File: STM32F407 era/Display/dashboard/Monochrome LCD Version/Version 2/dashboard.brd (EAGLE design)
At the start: 200 x 75.1 mm, 89 parts, among them IC2 74HC14D, IC3 74HC14D, U1 CAT4238TD-GT3

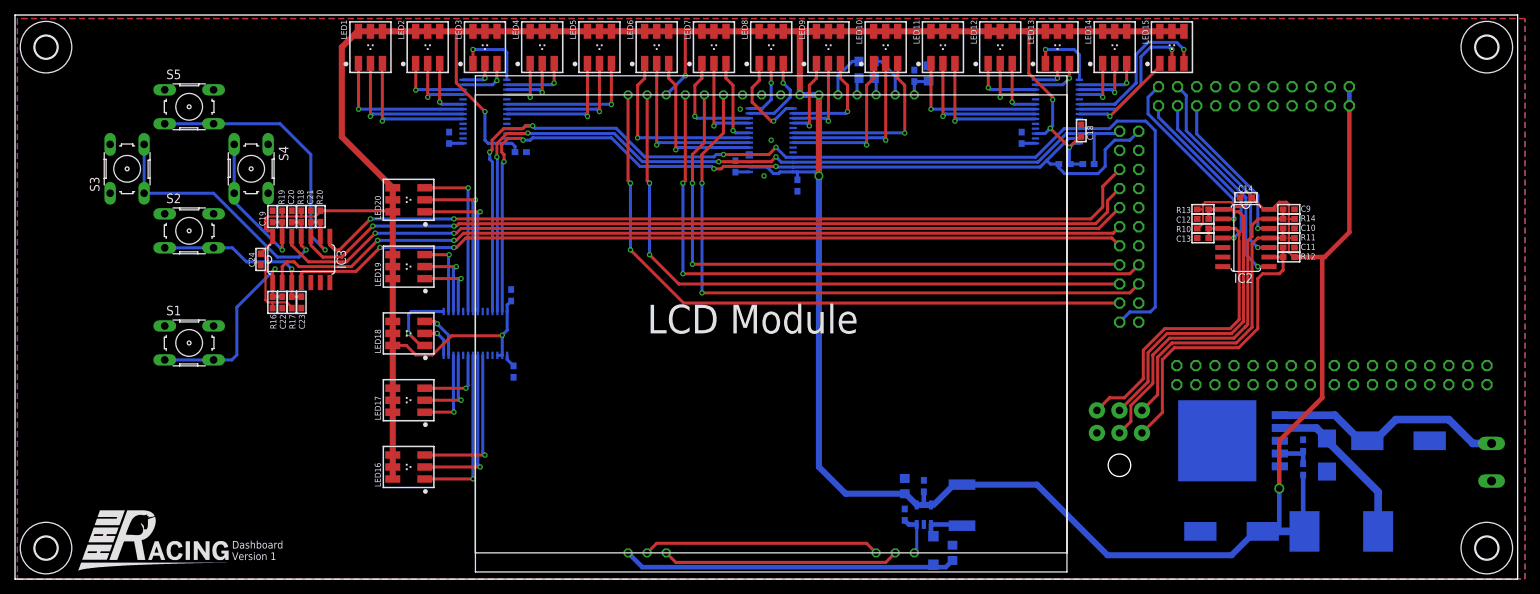
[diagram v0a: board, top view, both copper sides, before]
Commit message: fixed silkscreen and added extra button for interface
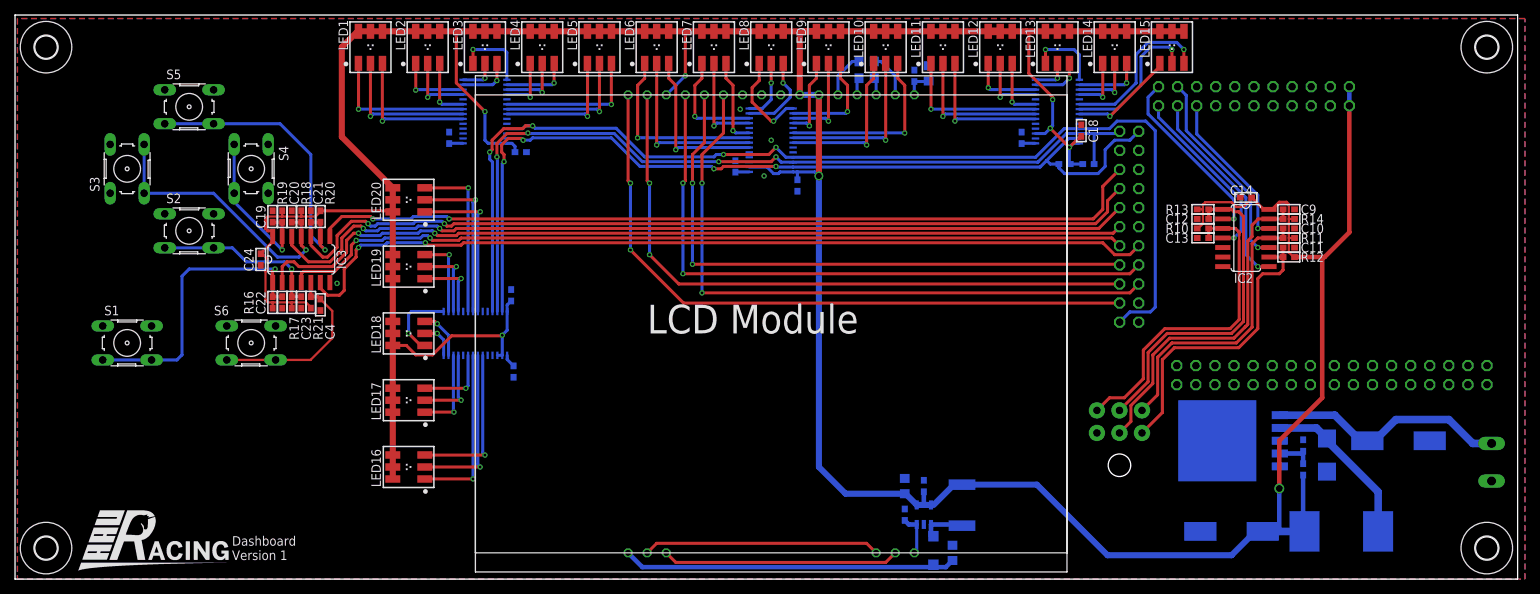
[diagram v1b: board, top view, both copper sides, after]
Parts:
- added C4: 100n, microbuilder:_0603
- added R21: 500, microbuilder:_0603
- added S6: (no value), switch-omron:B3F-10XX
- moved S1 8.26 mm to (58.1, 47.9)
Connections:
- new net SW6: C4.2, IC3.5, R21.1, S6.3, S6.4
- new net SW6S: IC3.6, U$1.P$10
- net 3.3V: now also R21.2
- net GND: now also C4.1, S6.1, S6.2; no longer IC3.5
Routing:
- net SW6S: track 0.00 -> 116.6 mm, vias 0 -> 2
- net SW6: track 0.00 -> 24.4 mm
- net SW1: track 28.5 -> 39.2 mm
- net 3.3V: track 543.4 -> 546.7 mm
- net SW3S: track 114.1 -> 116.1 mm
- net SW4S: track 115.3 -> 117.3 mm
- net SW1S: track 116.3 -> 118.0 mm
- net SW2S: track 112.5 -> 113.8 mm
- net SW5S: track 112.6 -> 111.7 mm

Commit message: started work on V2
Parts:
- moved U$42 5.46 mm to (193.4, 33.0), turned to 90 degrees
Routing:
- net BTN5: track 40.7 -> 53.8 mm
- net BTN3: track 39.0 -> 49.5 mm
- net BTN4: track 45.7 -> 54.4 mm
- net BTN1: track 47.3 -> 53.4 mm
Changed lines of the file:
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@@
 <attribute name="VALUE" x="166.4335" y="85.4074" size="0.4064" layer="28" ratio="10" rot="MR270"/>
 </element>
-<element name="U$42" library="unicorn" package="MICROFIT6SOCK" value="MICROFIT6" x="190.1825" y="37.465" rot="MR0"/>
+<element name="U$42" library="unicorn" package="MICROFIT6SOCK" value="MICROFIT6" x="193.3575" y="33.02" rot="MR90"/>
 <element name="R10" library="microbuilder" package="_0603" value="500" x="201.295" y="63.1825" smashed="yes" rot="R180">
 <attribute name="NAME" x="199.39" y="63.8175" size="1.27" layer="25" ratio="18" rot="R180"/>
@@
 <wire x1="205.74" y1="47.9425" x2="197.1675" y2="47.9425" width="0.4064" layer="1"/>
 <wire x1="197.1675" y1="47.9425" x2="195.2625" y2="46.0375" width="0.4064" layer="1"/>
-<wire x1="195.2625" y1="46.0375" x2="195.2625" y2="41.045" width="0.4064" layer="1"/>
-<wire x1="195.2625" y1="41.045" x2="193.1825" y2="38.965" width="0.4064" layer="1"/>
+<wire x1="195.2625" y1="46.0375" x2="195.2625" y2="39.6875" width="0.4064" layer="1"/>
 <wire x1="207.8355" y1="50.038" x2="205.74" y2="47.9425" width="0.4064" layer="1"/>
 <wire x1="210.0834" y1="61.9125" x2="208.5975" y2="61.9125" width="0.4064" layer="1"/>
 <wire x1="208.5975" y1="61.9125" x2="207.8355" y2="61.1505" width="0.4064" layer="1"/>
 <wire x1="207.8355" y1="61.1505" x2="207.8355" y2="50.038" width="0.4064" layer="1"/>
+<wire x1="195.2625" y1="39.6875" x2="197.8025" y2="37.1475" width="0.4064" layer="1"/>
+<wire x1="197.8025" y1="37.1475" x2="197.8025" y2="32.7025" width="0.4064" layer="1"/>
+<wire x1="197.8025" y1="32.7025" x2="195.58" y2="30.48" width="0.4064" layer="1"/>
+<wire x1="195.58" y1="30.48" x2="195.3175" y2="30.48" width="0.4064" layer="1"/>
+<wire x1="195.3175" y1="30.48" x2="194.8575" y2="30.02" width="0.4064" layer="1"/>
 </signal>
 <signal name="BTN2">
@@
 <wire x1="203.9366" y1="63.1825" x2="202.057" y2="63.1825" width="0.3048" layer="1"/>
 <wire x1="202.057" y1="63.1825" x2="202.057" y2="61.9125" width="0.4064" layer="1"/>
-<wire x1="187.1825" y1="38.965" x2="188.8575" y2="40.64" width="0.4064" layer="1"/>
-<wire x1="188.8575" y1="40.64" x2="190.8175" y2="40.64" width="0.4064" layer="1"/>
-<wire x1="190.8175" y1="40.64" x2="193.3575" y2="43.18" width="0.4064" layer="1"/>
-<wire x1="193.3575" y1="43.18" x2="193.3575" y2="46.99" width="0.4064" layer="1"/>
 <wire x1="193.3575" y1="46.99" x2="196.215" y2="49.8475" width="0.4064" layer="1"/>
 <wire x1="196.215" y1="49.8475" x2="204.9145" y2="49.8475" width="0.4064" layer="1"/>
@@
 <wire x1="206.121" y1="62.2935" x2="206.121" y2="61.5315" width="0.3048" layer="1"/>
 <wire x1="206.121" y1="61.5315" x2="206.121" y2="51.054" width="0.4064" layer="1"/>
+<wire x1="193.3575" y1="46.99" x2="193.3575" y2="37.52" width="0.4064" layer="1"/>
+<wire x1="193.3575" y1="37.52" x2="194.8575" y2="36.02" width="0.4064" layer="1"/>
 </signal>
 <signal name="BTN1">
@@
 <wire x1="205.105" y1="49.2125" x2="196.5325" y2="49.2125" width="0.4064" layer="1"/>
 <wire x1="196.5325" y1="49.2125" x2="193.9925" y2="46.6725" width="0.4064" layer="1"/>
-<wire x1="193.9925" y1="46.6725" x2="193.9925" y2="42.775" width="0.4064" layer="1"/>
-<wire x1="193.9925" y1="42.775" x2="190.1825" y2="38.965" width="0.4064" layer="1"/>
+<wire x1="193.9925" y1="46.6725" x2="193.9925" y2="39.0525" width="0.4064" layer="1"/>
 <wire x1="206.6925" y1="50.8" x2="205.105" y2="49.2125" width="0.4064" layer="1"/>
 <wire x1="206.6925" y1="50.8" x2="206.6925" y2="64.77" width="0.4064" layer="1"/>
 <wire x1="206.6925" y1="64.77" x2="206.0575" y2="65.405" width="0.4064" layer="1"/>
+<wire x1="193.9925" y1="39.0525" x2="196.5325" y2="36.5125" width="0.4064" layer="1"/>
+<wire x1="196.5325" y1="36.5125" x2="196.5325" y2="34.695" width="0.4064" layer="1"/>
+<wire x1="196.5325" y1="34.695" x2="194.8575" y2="33.02" width="0.4064" layer="1"/>
 </signal>
 <signal name="BTN4">
@@
 <wire x1="205.4225" y1="48.5775" x2="196.85" y2="48.5775" width="0.4064" layer="1"/>
 <wire x1="196.85" y1="48.5775" x2="194.6275" y2="46.355" width="0.4064" layer="1"/>
-<wire x1="194.6275" y1="46.355" x2="194.6275" y2="42.545" width="0.4064" layer="1"/>
-<wire x1="194.6275" y1="42.545" x2="191.7065" y2="39.624" width="0.4064" layer="1"/>
-<wire x1="191.7065" y1="39.624" x2="191.7065" y2="37.489" width="0.4064" layer="1"/>
-<wire x1="191.7065" y1="37.489" x2="190.1825" y2="35.965" width="0.4064" layer="1"/>
-<wire x1="207.01" y1="50.165" x2="206.91475" y2="50.06975" width="0.4064" layer="1"/>
-<wire x1="206.91475" y1="50.06975" x2="205.4225" y2="48.5775" width="0.4064" layer="1"/>
+<wire x1="194.6275" y1="46.355" x2="194.6275" y2="39.37" width="0.4064" layer="1"/>
+<wire x1="207.264" y1="50.419" x2="205.4225" y2="48.5775" width="0.4064" layer="1"/>
 <wire x1="210.0834" y1="64.4525" x2="208.661" y2="64.4525" width="0.4064" layer="1"/>
 <wire x1="208.661" y1="64.4525" x2="207.8355" y2="63.627" width="0.4064" layer="1"/>
@@
 <wire x1="207.8355" y1="62.103" x2="207.264" y2="61.5315" width="0.4064" layer="1"/>
 <wire x1="207.264" y1="61.5315" x2="207.264" y2="50.419" width="0.4064" layer="1"/>
-<wire x1="207.264" y1="50.419" x2="207.01" y2="50.165" width="0.4064" layer="1"/>
+<wire x1="194.6275" y1="39.37" x2="197.1675" y2="36.83" width="0.4064" layer="1"/>
+<wire x1="197.1675" y1="36.83" x2="197.1675" y2="33.02" width="0.4064" layer="1"/>
+<wire x1="197.1675" y1="33.02" x2="195.67525" y2="31.52775" width="0.4064" layer="1"/>
+<wire x1="195.67525" y1="31.52775" x2="193.34975" y2="31.52775" width="0.4064" layer="1"/>
+<wire x1="193.34975" y1="31.52775" x2="191.8575" y2="33.02" width="0.4064" layer="1"/>
 </signal>
 <signal name="BTN5">
@@
 <wire x1="206.0575" y1="47.3075" x2="197.485" y2="47.3075" width="0.4064" layer="1"/>
 <wire x1="197.485" y1="47.3075" x2="195.8975" y2="45.72" width="0.4064" layer="1"/>
-<wire x1="195.8975" y1="45.72" x2="195.8975" y2="38.68" width="0.4064" layer="1"/>
-<wire x1="195.8975" y1="38.68" x2="193.1825" y2="35.965" width="0.4064" layer="1"/>
+<wire x1="195.8975" y1="45.72" x2="195.8975" y2="39.95" width="0.4064" layer="1"/>
 <wire x1="206.0575" y1="47.3075" x2="208.5975" y2="49.8475" width="0.4064" layer="1"/>
 <wire x1="208.5975" y1="49.8475" x2="208.5975" y2="56.515" width="0.4064" layer="1"/>
@@
 <wire x1="211.455" y1="57.15" x2="211.963" y2="57.658" width="0.4064" layer="1"/>
 <wire x1="211.963" y1="57.658" x2="211.963" y2="59.3725" width="0.4064" layer="1"/>
+<wire x1="195.8975" y1="39.95" x2="195.9525" y2="39.95" width="0.4064" layer="1"/>
+<wire x1="195.9525" y1="39.95" x2="198.4375" y2="37.465" width="0.4064" layer="1"/>
+<wire x1="198.4375" y1="37.465" x2="198.4375" y2="31.4325" width="0.4064" layer="1"/>
+<wire x1="198.4375" y1="31.4325" x2="195.2625" y2="28.2575" width="0.4064" layer="1"/>
+<wire x1="195.2625" y1="28.2575" x2="193.62" y2="28.2575" width="0.4064" layer="1"/>
+<wire x1="193.62" y1="28.2575" x2="191.8575" y2="30.02" width="0.4064" layer="1"/>
 </signal>
 <signal name="N$54">
@@
 </signal>
 </signals>
-<errors>
-</errors>
 </board>
 </drawing>

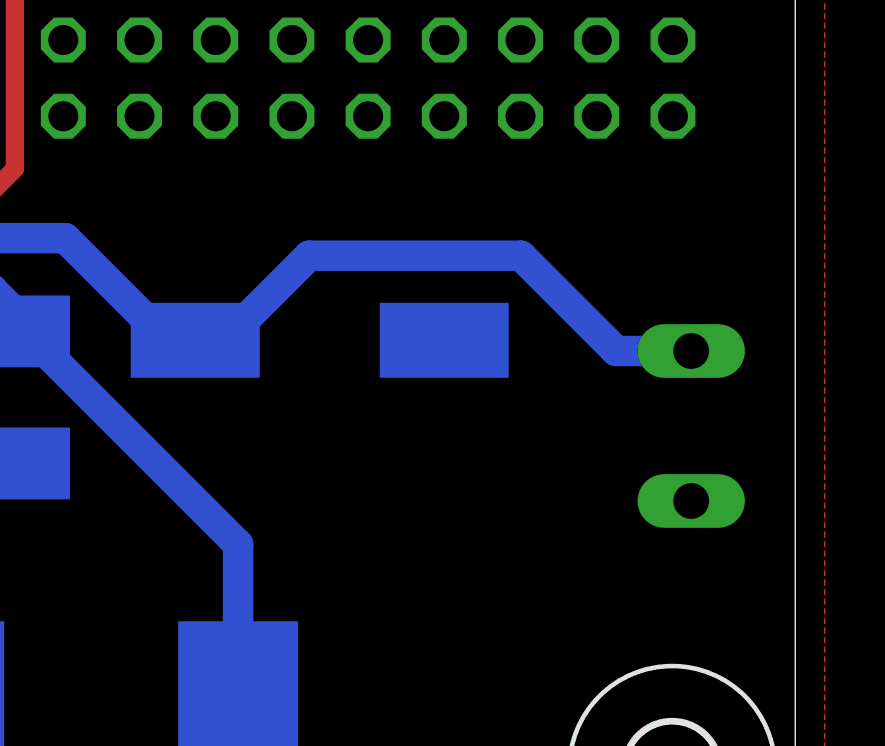
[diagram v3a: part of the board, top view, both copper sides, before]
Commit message: adding last changes to accomendate changes in H-Bridge
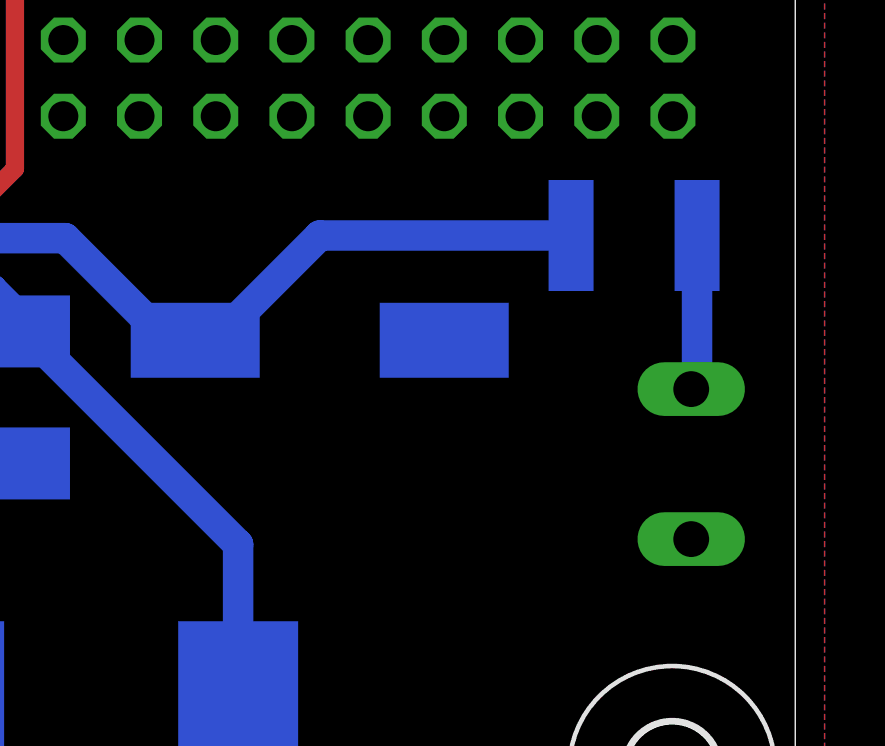
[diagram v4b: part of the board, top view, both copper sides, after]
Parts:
- added PTC1: (no value), microbuilder:PTC1812
- moved X1 1.27 mm to (238.4, 30.8)
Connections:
- new net N$77: C25.+, IC1.1, PTC1.P$1
- net 12V: now also PTC1.P$2; no longer C25.+, IC1.1
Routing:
- net N$77: track 0.00 -> 27.2 mm
- net 12V: track 31.9 -> 5.31 mm
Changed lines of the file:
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@@
 <attribute name="VALUE" x="162.6552" y="27.6225" size="0.4064" layer="28" ratio="10" rot="MR90"/>
 </element>
-<element name="X1" library="con-wago-500" package="W237-102" value="" x="238.4425" y="32.0675" smashed="yes" rot="MR270">
-<attribute name="OC_NEWARK" value="70K9898" x="238.4425" y="32.0675" size="1.778" layer="28" rot="MR270" display="off"/>
-<attribute name="MPN" value="237-102" x="238.4425" y="32.0675" size="1.778" layer="28" rot="MR270" display="off"/>
-<attribute name="MF" value="" x="238.4425" y="32.0675" size="1.778" layer="28" rot="MR270" display="off"/>
-<attribute name="OC_FARNELL" value="unknown" x="238.4425" y="32.0675" size="1.778" layer="28" rot="MR270" display="off"/>
-<attribute name="VALUE" x="246.0625" y="37.1075" size="1.27" layer="28" ratio="10" rot="MR270"/>
-<attribute name="NAME" x="234.5963" y="38.6588" size="1.27" layer="26" ratio="10" rot="MR180"/>
+<element name="X1" library="con-wago-500" package="W237-102" value="" x="238.4425" y="30.7975" smashed="yes" rot="MR270">
+<attribute name="OC_NEWARK" value="70K9898" x="238.4425" y="30.7975" size="1.778" layer="28" rot="MR270" display="off"/>
+<attribute name="MPN" value="237-102" x="238.4425" y="30.7975" size="1.778" layer="28" rot="MR270" display="off"/>
+<attribute name="MF" value="" x="238.4425" y="30.7975" size="1.778" layer="28" rot="MR270" display="off"/>
+<attribute name="OC_FARNELL" value="unknown" x="238.4425" y="30.7975" size="1.778" layer="28" rot="MR270" display="off"/>
+<attribute name="VALUE" x="246.0625" y="35.8375" size="1.27" layer="28" ratio="10" rot="MR270"/>
+<attribute name="NAME" x="234.5963" y="37.3888" size="1.27" layer="26" ratio="10" rot="MR180"/>
 </element>
 <element name="LED1" library="microbuilder" package="RGBLED_PLCC6" value="" x="90.4875" y="87.3125" smashed="yes">
@@
 <attribute name="VALUE" x="85.3123" y="51.7525" size="0.4064" layer="27" ratio="10" rot="R90"/>
 </element>
+<element name="PTC1" library="microbuilder" package="PTC1812" value="" x="237.8075" y="38.4175" rot="MR180"/>
 </elements>
 <signals>
@@
 <signal name="12V">
 <contactref element="X1" pad="1"/>
-<contactref element="IC1" pad="1"/>
-<contactref element="C25" pad="+"/>
-<wire x1="211.5312" y1="38.3286" x2="218.8464" y2="38.3286" width="1.016" layer="16"/>
-<wire x1="218.8464" y1="38.3286" x2="221.615" y2="35.56" width="1.016" layer="16"/>
-<wire x1="221.615" y1="35.56" x2="223.18" y2="34.925" width="1.016" layer="16"/>
-<wire x1="226.9725" y1="37.7425" x2="224.155" y2="34.925" width="1.016" layer="16"/>
-<wire x1="224.155" y1="34.925" x2="223.18" y2="34.925" width="1.016" layer="16"/>
-<wire x1="226.9725" y1="37.7425" x2="234.0375" y2="37.7425" width="1.016" layer="16"/>
-<wire x1="234.0375" y1="37.7425" x2="237.2125" y2="34.5675" width="1.016" layer="16"/>
-<wire x1="237.2125" y1="34.5675" x2="239.7125" y2="34.5675" width="1.016" layer="16"/>
+<contactref element="PTC1" pad="P$2"/>
+<wire x1="239.9075" y1="38.4175" x2="239.9075" y2="33.2975" width="1.016" layer="16"/>
+<wire x1="239.9075" y1="33.2975" x2="239.7125" y2="33.2975" width="1.016" layer="16"/>
 </signal>
 <signal name="N$7">
@@
 <wire x1="102.5525" y1="60.96" x2="102.87" y2="61.2775" width="0.4064" layer="1"/>
 </signal>
+<signal name="N$77">
+<contactref element="IC1" pad="1"/>
+<contactref element="C25" pad="+"/>
+<wire x1="211.5312" y1="38.3286" x2="218.8464" y2="38.3286" width="1.016" layer="16"/>
+<wire x1="218.8464" y1="38.3286" x2="221.615" y2="35.56" width="1.016" layer="16"/>
+<wire x1="221.615" y1="35.56" x2="223.18" y2="34.925" width="1.016" layer="16"/>
+<contactref element="PTC1" pad="P$1"/>
+<wire x1="235.7075" y1="38.4175" x2="227.33" y2="38.4175" width="1.016" layer="16"/>
+<wire x1="227.33" y1="38.4175" x2="223.52" y2="34.6075" width="1.016" layer="16"/>
+<wire x1="223.52" y1="34.6075" x2="223.4975" y2="34.6075" width="1.016" layer="16"/>
+<wire x1="223.4975" y1="34.6075" x2="223.18" y2="34.925" width="1.016" layer="16"/>
+</signal>
 </signals>
-<errors>
-</errors>
 </board>
 </drawing>
